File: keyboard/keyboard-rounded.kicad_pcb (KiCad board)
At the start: 2 copper layers, 134.3 x 93.3 mm, 40 parts

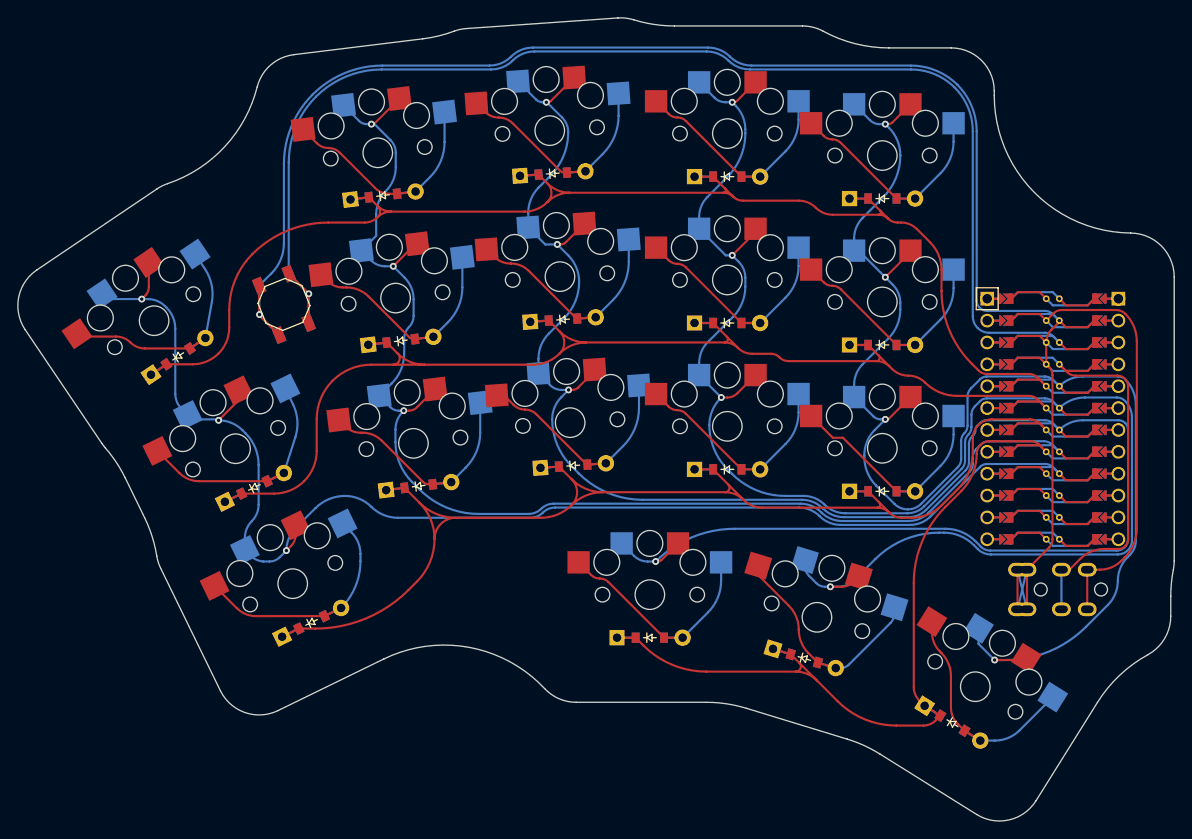
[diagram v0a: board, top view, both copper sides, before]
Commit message: Fix some DRC issues in rounded PCB
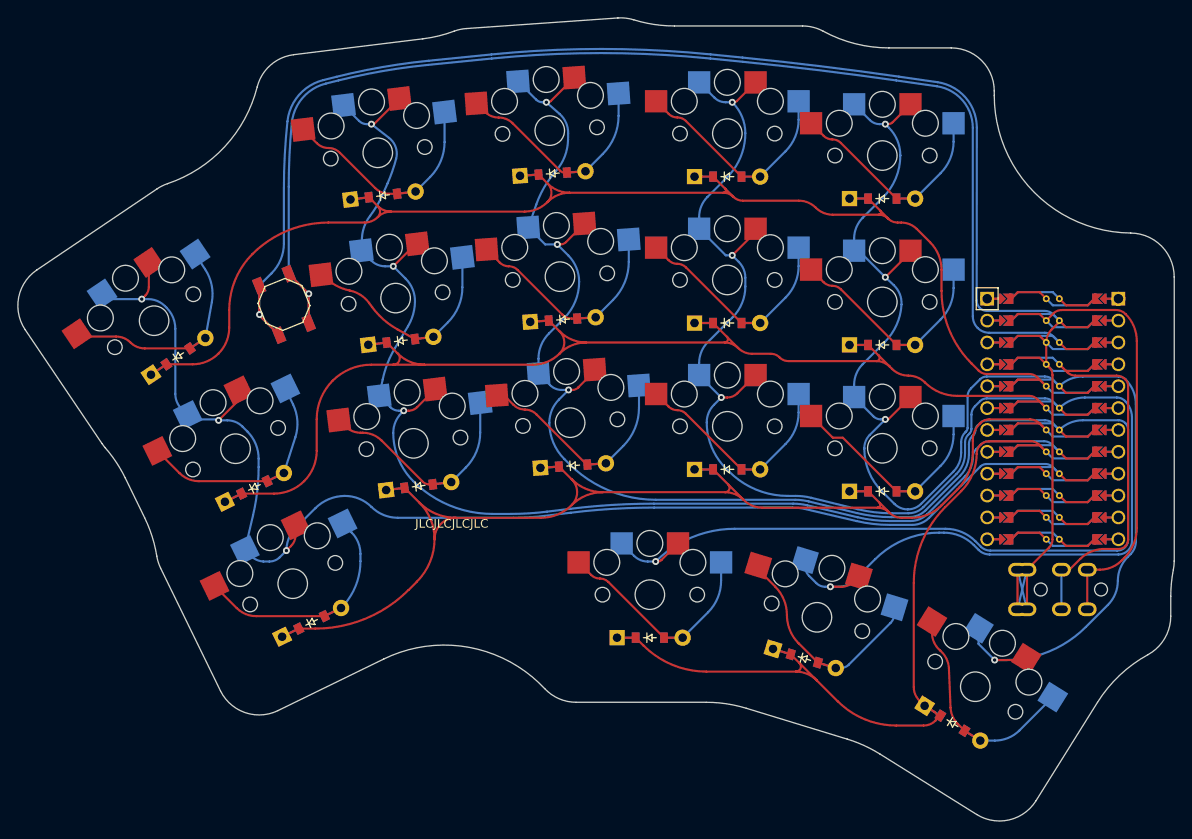
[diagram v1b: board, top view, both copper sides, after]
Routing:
- net F7: track 150.2 -> 148.7 mm
- net middle_home: track 26.7 -> 28.0 mm
- net reachy_thumb: track 27.2 -> 28.4 mm
- net resty_thumb: track 26.1 -> 27.1 mm
- net RST: track 149.9 -> 148.9 mm
- net GND: track 200.4 -> 199.6 mm
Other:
- board text added: "JLCJLCJLCJLC"
